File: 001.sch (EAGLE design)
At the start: 27 parts, among them CN01 PWR5V, CN02 JD-VCC, CN03 TO-RLY, CN04 I2C-LCD, CN05 INPUT-A, CN06 INPUT-B, CN07 BUTTON-A, CN08 BUTTON-B, CN09 BUTTON-STOP, CN10 DELAY-VR, M1 ARDUINO-NANO-3.0

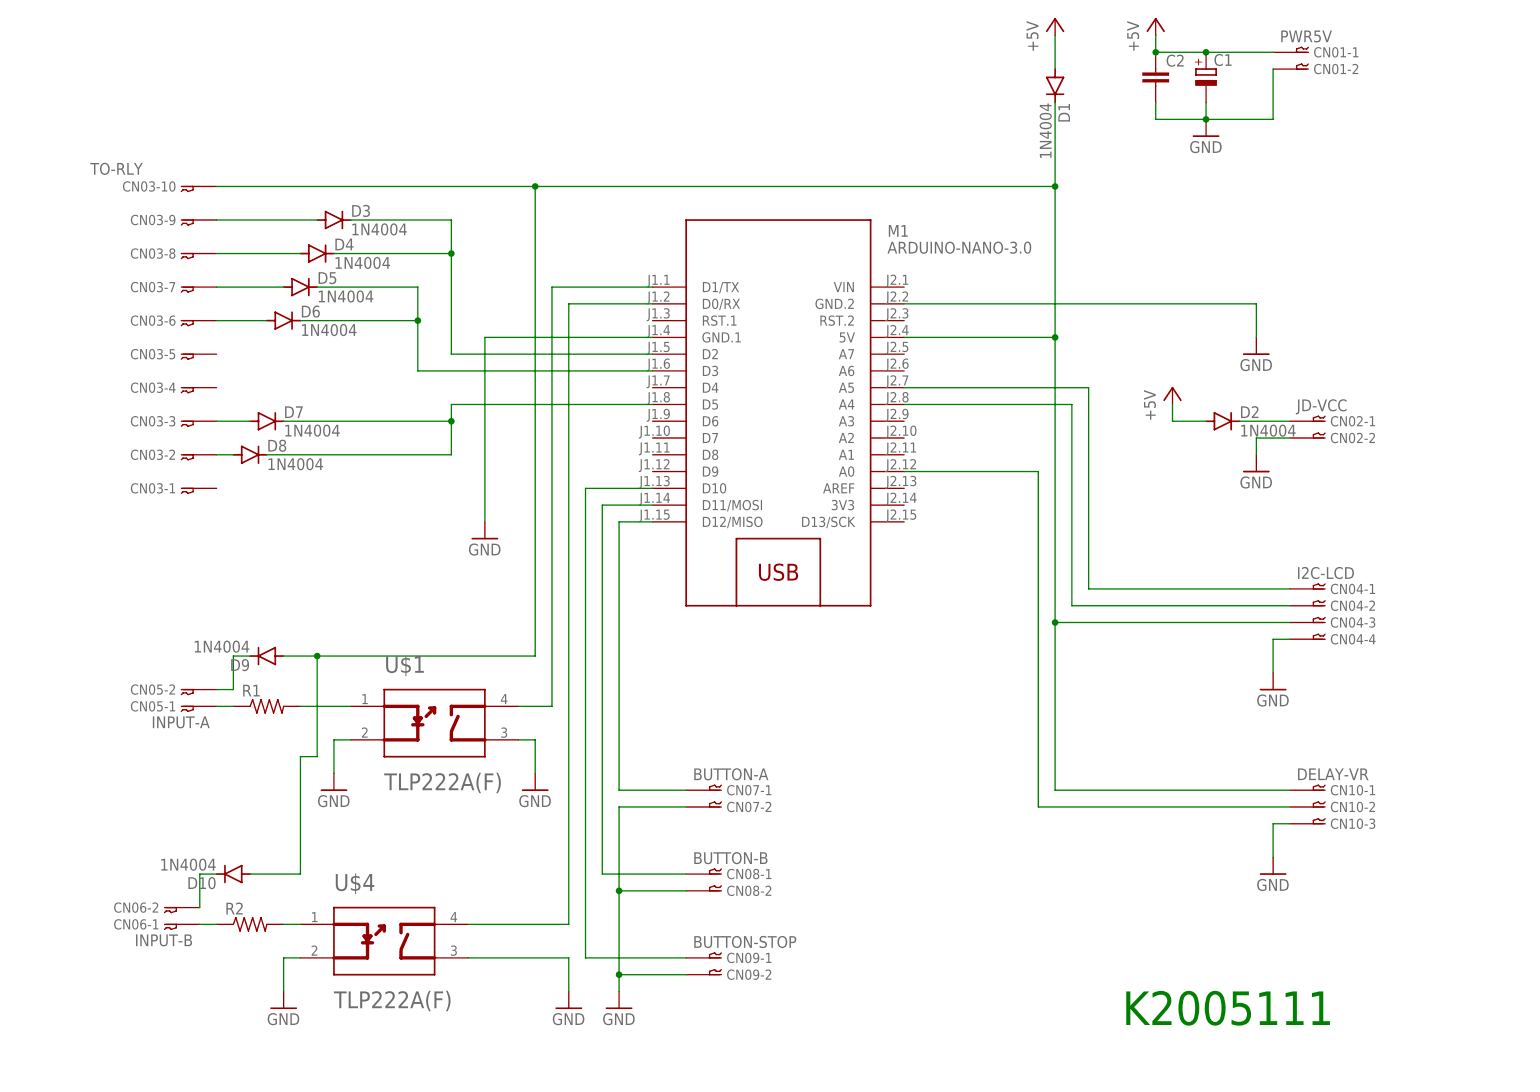
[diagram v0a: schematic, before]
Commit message: 1N4007に変更
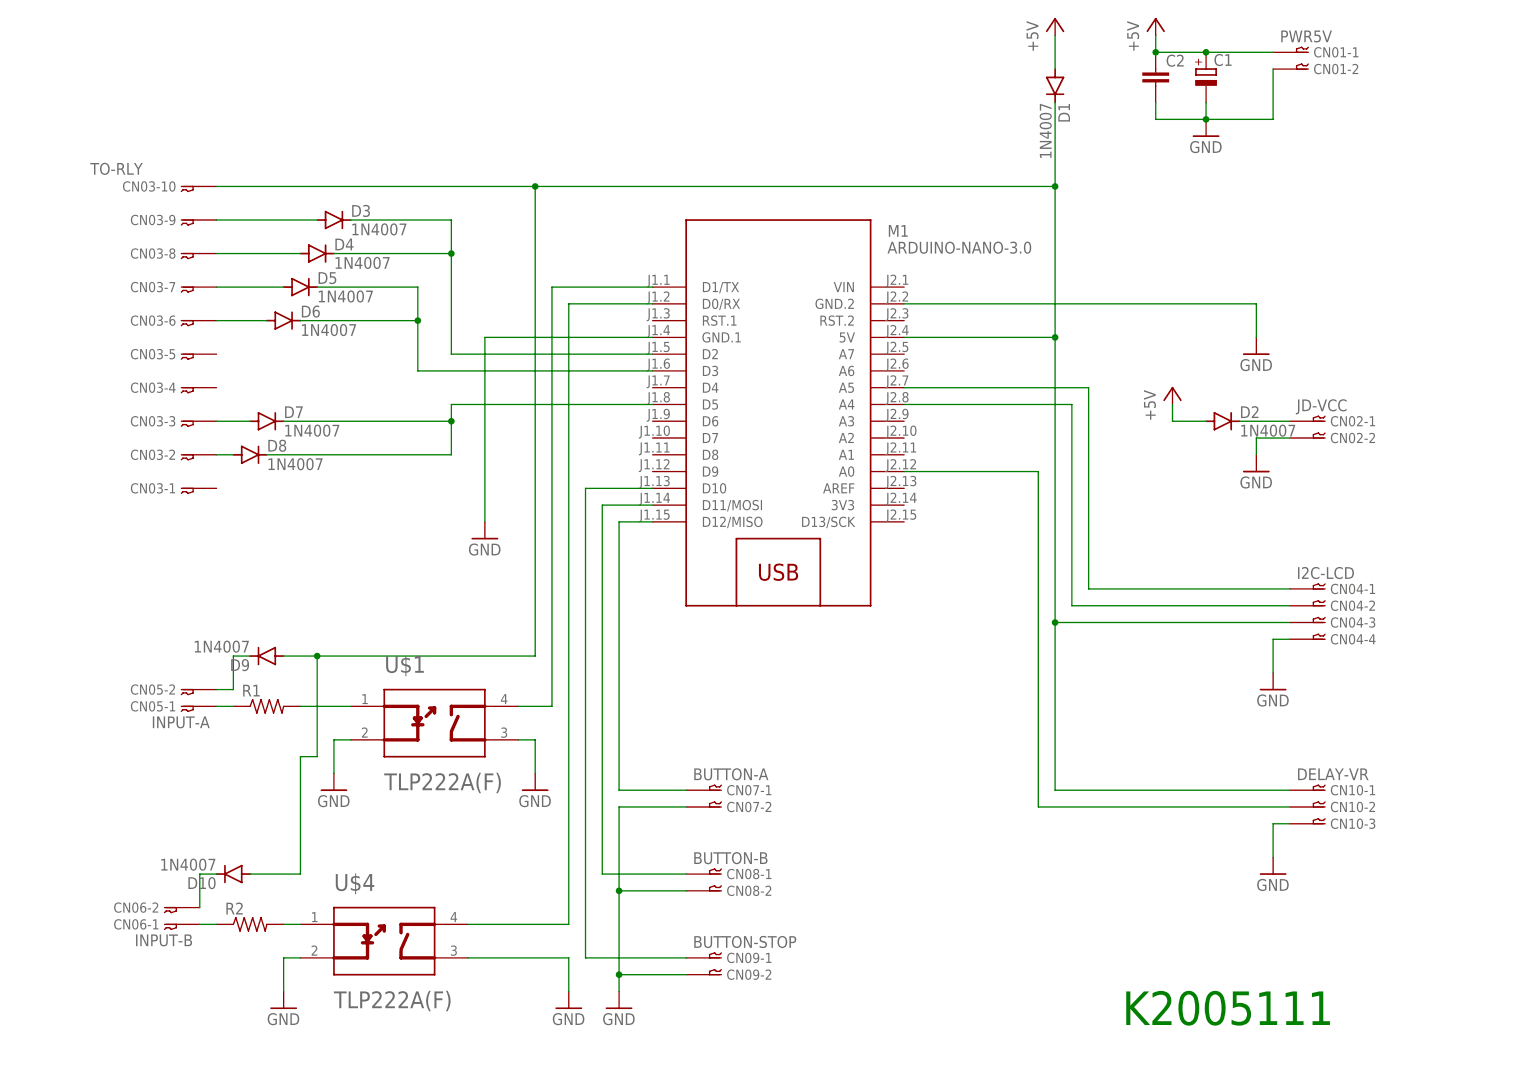
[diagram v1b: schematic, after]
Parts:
- D1, D10, D2, D3, D4, D5, D6, D7, D8, D9: value 1N4004 -> 1N4007
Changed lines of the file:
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@@
 <part name="CN02" library="holly" deviceset="02-JST" device="-A" value="JD-VCC"/>
 <part name="CN07" library="holly" deviceset="02-JST" device="-A" value="BUTTON-A"/>
-<part name="D1" library="diode" library_urn="urn:adsk.eagle:library:210" deviceset="1N4004" device="" package3d_urn="urn:adsk.eagle:package:43336/1"/>
-<part name="D2" library="diode" library_urn="urn:adsk.eagle:library:210" deviceset="1N4004" device="" package3d_urn="urn:adsk.eagle:package:43336/1"/>
-<part name="D3" library="diode" library_urn="urn:adsk.eagle:library:210" deviceset="1N4004" device="" package3d_urn="urn:adsk.eagle:package:43336/1"/>
-<part name="D4" library="diode" library_urn="urn:adsk.eagle:library:210" deviceset="1N4004" device="" package3d_urn="urn:adsk.eagle:package:43336/1"/>
-<part name="D5" library="diode" library_urn="urn:adsk.eagle:library:210" deviceset="1N4004" device="" package3d_urn="urn:adsk.eagle:package:43336/1"/>
+<part name="D1" library="diode" library_urn="urn:adsk.eagle:library:210" deviceset="1N4004" device="" package3d_urn="urn:adsk.eagle:package:43336/1" value="1N4007"/>
+<part name="D2" library="diode" library_urn="urn:adsk.eagle:library:210" deviceset="1N4004" device="" package3d_urn="urn:adsk.eagle:package:43336/1" value="1N4007"/>
+<part name="D3" library="diode" library_urn="urn:adsk.eagle:library:210" deviceset="1N4004" device="" package3d_urn="urn:adsk.eagle:package:43336/1" value="1N4007"/>
+<part name="D4" library="diode" library_urn="urn:adsk.eagle:library:210" deviceset="1N4004" device="" package3d_urn="urn:adsk.eagle:package:43336/1" value="1N4007"/>
+<part name="D5" library="diode" library_urn="urn:adsk.eagle:library:210" deviceset="1N4004" device="" package3d_urn="urn:adsk.eagle:package:43336/1" value="1N4007"/>
 <part name="M1" library="diy-modules" deviceset="ARDUINO-NANO-3.0" device=""/>
 <part name="C1" library="rcl" library_urn="urn:adsk.eagle:library:334" deviceset="CPOL-EU" device="E2-5" package3d_urn="urn:adsk.eagle:package:23346/2"/>
@@
 <part name="CN04" library="holly" deviceset="04-JST" device="-A" value="I2C-LCD"/>
 <part name="GND3" library="supply1" library_urn="urn:adsk.eagle:library:371" deviceset="GND" device=""/>
-<part name="D6" library="diode" library_urn="urn:adsk.eagle:library:210" deviceset="1N4004" device="" package3d_urn="urn:adsk.eagle:package:43336/1"/>
-<part name="D7" library="diode" library_urn="urn:adsk.eagle:library:210" deviceset="1N4004" device="" package3d_urn="urn:adsk.eagle:package:43336/1"/>
-<part name="D8" library="diode" library_urn="urn:adsk.eagle:library:210" deviceset="1N4004" device="" package3d_urn="urn:adsk.eagle:package:43336/1"/>
+<part name="D6" library="diode" library_urn="urn:adsk.eagle:library:210" deviceset="1N4004" device="" package3d_urn="urn:adsk.eagle:package:43336/1" value="1N4007"/>
+<part name="D7" library="diode" library_urn="urn:adsk.eagle:library:210" deviceset="1N4004" device="" package3d_urn="urn:adsk.eagle:package:43336/1" value="1N4007"/>
+<part name="D8" library="diode" library_urn="urn:adsk.eagle:library:210" deviceset="1N4004" device="" package3d_urn="urn:adsk.eagle:package:43336/1" value="1N4007"/>
 <part name="GND4" library="supply1" library_urn="urn:adsk.eagle:library:371" deviceset="GND" device=""/>
 <part name="GND5" library="supply1" library_urn="urn:adsk.eagle:library:371" deviceset="GND" device=""/>
 <part name="R1" library="rcl" library_urn="urn:adsk.eagle:library:334" deviceset="R-US_" device="0207/7" package3d_urn="urn:adsk.eagle:package:23493/2"/>
 <part name="R2" library="rcl" library_urn="urn:adsk.eagle:library:334" deviceset="R-US_" device="0207/7" package3d_urn="urn:adsk.eagle:package:23493/2"/>
-<part name="D9" library="diode" library_urn="urn:adsk.eagle:library:210" deviceset="1N4004" device="" package3d_urn="urn:adsk.eagle:package:43336/1"/>
-<part name="D10" library="diode" library_urn="urn:adsk.eagle:library:210" deviceset="1N4004" device="" package3d_urn="urn:adsk.eagle:package:43336/1"/>
+<part name="D9" library="diode" library_urn="urn:adsk.eagle:library:210" deviceset="1N4004" device="" package3d_urn="urn:adsk.eagle:package:43336/1" value="1N4007"/>
+<part name="D10" library="diode" library_urn="urn:adsk.eagle:library:210" deviceset="1N4004" device="" package3d_urn="urn:adsk.eagle:package:43336/1" value="1N4007"/>
 <part name="GND6" library="supply1" library_urn="urn:adsk.eagle:library:371" deviceset="GND" device=""/>
 <part name="GND7" library="supply1" library_urn="urn:adsk.eagle:library:371" deviceset="GND" device=""/>

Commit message: ソースコードと一緒に管理
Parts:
- removed D4, D5, D6, D7, D8: 1N4007, diode:1N4004
- added CN11: INPUT-B, holly:02-JST-A
- added CN12: BUTTON-C, holly:02-JST-A
- added R3: (no value), rcl:R-US_0207/7
- added U$2: (no value), Toshiba-TLP222AF:TOSHIBA_TLP222A_F_SIMPLE
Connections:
- net +5V renamed N$10
- removed net N$10 (its old number): CN03-2.1, D8.A
- removed net N$15: D7.C, D8.C, M1.D5
- new net N$1: CN03-4.1, CN03-5.1, M1.D4
- new net N$12: CN11-2.1, D3.C
- net 5V: now also D3.A
- net GND: now also CN12-2.1, U$2.1_DRAIN, U$2.CATHODE
- net N$11: now also CN03-6.1, CN03-7.1; no longer D5.C, D6.C
- net N$14: now also CN03-8.1, CN03-9.1; no longer D3.C, D4.C
- net N$3: now also CN03-2.1, CN03-3.1, M1.D5; no longer CN03-9.1, D3.A
- net N$6: now also M1.D9, U$2.2_DRAIN; no longer CN03-8.1, D4.A
- net N$7: now also CN11-1.1, R3.1; no longer CN03-7.1, D5.A
- net N$8: now also R3.2, U$2.ANODE; no longer CN03-6.1, D6.A
- net N$9: now also CN12-1.1, M1.D13/SCK; no longer CN03-3.1, D7.A
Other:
- moved on the sheet: C1, C2, CN01-1, CN01-2, CN02-1, CN02-2, CN03-1, CN03-10, CN03-2, CN03-3, CN03-4, CN03-5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

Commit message: CAM初版
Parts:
- removed D9: 1N4007, diode:1N4004
- removed U$4: (no value), Toshiba-TLP222AF:TOSHIBA_TLP222A_F_SIMPLE
- added D5: 1N4007, diode:1N4004
- added U$3: (no value), Toshiba-TLP222AF:TOSHIBA_TLP222A_F_SIMPLE
- C1: value (none) -> 10uF
- C2: value (none) -> 0.1uF
- CN07: value BUTTON-A -> INPUT-C
- CN08: value BUTTON-B -> BTN-A
- CN09: value BUTTON-STOP -> BTN-B
- CN10: value DELAY-VR -> BTN-C; device holly:03-JST-A -> holly:02-JST-A
- CN11: value INPUT-B -> BTN-STOP
- CN12: value BUTTON-C -> DELAY-VR; device holly:02-JST-A -> holly:03-JST-A
- R1, R2, R3: value (none) -> 4.7k
- U$1: value (none) -> U1
- renumbered D10 to D4
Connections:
- net N$10 renamed 5V_M
- net N$2 renamed 5V_B
- net 5V: now also CN12-1.1, D5.A; no longer CN10-1.1, D9.A
- net GND: now also CN10-2.1, CN11-2.1, CN12-3.1, U$3.1_DRAIN, U$3.CATHODE; no longer CN07-2.1, CN10-3.1, CN12-2.1, U$4.1_DRAIN, U$4.CATHODE
- net N$12: now also CN07-2.1, D5.C; no longer CN11-2.1, D3.C
- net N$17: now also U$2.2_DRAIN; no longer U$4.2_DRAIN
- net N$20: now also U$2.ANODE; no longer U$4.ANODE
- net N$24: now also D3.C; no longer D9.C
- net N$25: now also CN11-1.1; no longer CN09-1.1
- net N$26: now also CN09-1.1; no longer CN08-1.1
- net N$27: now also CN08-1.1; no longer CN07-1.1
- net N$29: now also CN12-2.1; no longer CN10-2.1
- net N$6: now also U$3.2_DRAIN; no longer U$2.2_DRAIN
- net N$7: now also CN07-1.1; no longer CN11-1.1
- net N$8: now also U$3.ANODE; no longer U$2.ANODE
- net N$9: now also CN10-1.1; no longer CN12-1.1
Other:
- note added: "MODEL-400 K2005111"
- note removed: "K2005111"
- moved on the sheet: C1, C2, CN07-1, CN07-2, CN08-1, CN08-2, CN09-1, CN09-2, CN10-1, CN10-2, CN11-1, CN11-2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

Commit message: ヴァリスタ追加
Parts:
- added U$4, U$5, U$6, U$7, U$8, U$9: TNR10V471K, holly:TNR10V471K
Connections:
- net GND: now also U$5.2, U$7.2, U$9.1
- net N$12: now also U$8.2
- net N$21: now also U$6.2, U$7.1
- net N$22: now also U$6.1
- net N$23: now also U$4.2, U$5.1
- net N$24: now also U$4.1
- net N$7: now also U$8.1, U$9.2
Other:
- moved on the sheet: CN05-1, CN05-2, CN06-1, CN06-2, CN07-1, CN07-2, D4
